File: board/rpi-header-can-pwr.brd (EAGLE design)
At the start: 65 x 56.5 mm, 31 parts, among them U1 MCP2515, X1 RJ45-8L21-S, X2 RJ45-8L21-S

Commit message: board - minor adjustments
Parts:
- removed JP3: (no value), pinhead:1X02
- added J1: (no value), SparkFun-Connectors:SCREWTERMINAL-3.5MM-2
- moved C4 2.83 mm to (55.8, 17.3), turned to 270 degrees
- moved C3 0.76 mm to (54.0, 17.4), turned to 270 degrees
- moved F3 0.50 mm to (53.5, 13.5), turned to 180 degrees
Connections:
- net GND: now also J1.1; no longer JP3.1
- net N$5: now also J1.2; no longer JP3.2
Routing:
- net N$5: track 5.37 -> 8.85 mm
- net +3V3: track 71.0 -> 67.8 mm
- net +12V: track 81.3 -> 84.0 mm
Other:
- board text added: "12V"
- board text added: "2020.05.08 v1.2"
- board text added: "FUSE 1.35A"
- board text added: "FUSE 2.5A"
- board text added: "GND"
- board text removed: "2020.05.03 v1.2"
- board text removed: "5V"
- board text removed: "5V enable"
- board text removed: "FUSE"
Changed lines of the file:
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@@
 <text x="33.1" y="44.5" size="0.8128" layer="121">C1</text>
 <text x="35.5" y="44.5" size="0.8128" layer="121">C2</text>
-<text x="56.7" y="16.2" size="0.8128" layer="121">C1</text>
-<text x="56.7" y="14.3" size="0.8128" layer="121">C2</text>
+<text x="53.5" y="14.5" size="0.8128" layer="121">C1</text>
+<text x="55.3" y="14.5" size="0.8128" layer="121">C2</text>
 <text x="5.3" y="12.2" size="0.8128" layer="121">shield</text>
 <text x="46.2" y="27.4" size="0.8128" layer="121">slope</text>
@@
 <circle x="36.8" y="34.2" radius="0.412309375" width="0.3048" layer="121"/>
 <text x="40.9" y="21.9" size="0.8128" layer="121">D2</text>
-<text x="11.6866" y="27.915" size="1.524" layer="200" font="vector" rot="R90">2020.05.03
+<text x="11.6866" y="27.915" size="1.524" layer="200" font="vector" rot="R90">2020.05.08
 v1.2</text>
 <rectangle x1="30.0314" y1="40.9822" x2="30.387" y2="41.033" layer="200" rot="R90"/>
@@
 <rectangle x1="12.3784" y1="44.0556" x2="12.5816" y2="44.1064" layer="200" rot="R90"/>
 <rectangle x1="12.4038" y1="45.5034" x2="12.5562" y2="45.5542" layer="200" rot="R90"/>
-<text x="4.5" y="41" size="1.016" layer="121" rot="R90">5V enable</text>
 <text x="16" y="46.5" size="1.016" layer="122" rot="MR180">C5</text>
 <text x="18.5" y="46.6" size="1.016" layer="122" rot="MR180">C5</text>
@@
 <wire x1="44" y1="4" x2="46" y2="4" width="0.4064" layer="121" curve="180"/>
 <wire x1="44" y1="19" x2="46" y2="19" width="0.4064" layer="121" curve="-180"/>
-<text x="3" y="44" size="1.016" layer="121">5V</text>
 <text x="9.2" y="32.3" size="0.8128" layer="121">R1</text>
-<text x="50.5" y="15" size="1.016" layer="121">FUSE</text>
+<text x="51.9" y="12.7" size="1.016" layer="121">FUSE
+1.35A</text>
 <polygon width="0.254" layer="29">
 <vertex x="16.5" y="38.5"/>
@@
 <wire x1="11.5" y1="37" x2="12" y2="36" width="0.254" layer="121"/>
 <wire x1="12" y1="36" x2="11" y2="36" width="0.254" layer="121"/>
+<text x="5" y="40.5" size="1.016" layer="121">FUSE
+2.5A</text>
+<text x="54" y="2" size="1.016" layer="121">12V</text>
+<text x="49.5" y="2" size="1.016" layer="121">GND</text>
 </plain>
 <attributes>
@@
 <attribute name="PROD_ID" value="CAP-07876" x="51.36" y="54.72" size="1.778" layer="27" rot="R270" display="off"/>
 </element>
-<element name="C3" library="rcl" package="C0603" value="100n" x="54.63" y="16.98"/>
-<element name="C4" library="rcl" package="C0603" value="1u" x="54.68" y="14.73"/>
+<element name="C3" library="rcl" package="C0603" value="100n" x="53.98" y="17.37" rot="R270"/>
+<element name="C4" library="rcl" package="C0603" value="1u" x="55.83" y="17.32" rot="R270"/>
 <element name="C6" library="rcl" package="C0603" value="1u" x="33.63" y="42.51" rot="R270"/>
 <element name="C8" library="rcl" package="C0603" value="100n" x="35.98" y="42.52" rot="R270"/>
@@
 <element name="D3" library="transistor" package="SOT23" value="BC846" x="8" y="38" rot="MR0"/>
 <element name="R4" library="rcl" package="R0603" value="1k" x="8" y="33" rot="MR270"/>
-<element name="JP3" library="pinhead" package="1X02" value="" x="53.5" y="5"/>
-<element name="F3" library="fuse" package="LITTLEFUSE" value="" x="53.5" y="13" rot="R135">
-<attribute name="OC_FARNELL" value="unknown" x="53.5" y="13" size="1.778" layer="27" rot="R135" display="off"/>
-<attribute name="MPN" value="" x="53.5" y="13" size="1.778" layer="27" rot="R135" display="off"/>
-<attribute name="OC_NEWARK" value="unknown" x="53.5" y="13" size="1.778" layer="27" rot="R135" display="off"/>
-<attribute name="MF" value="" x="53.5" y="13" size="1.778" layer="27" rot="R135" display="off"/>
+<element name="F3" library="fuse" package="LITTLEFUSE" value="" x="53.5" y="13.5" rot="R180">
+<attribute name="OC_FARNELL" value="unknown" x="53.5" y="13.5" size="1.778" layer="27" rot="R180" display="off"/>
+<attribute name="MPN" value="" x="53.5" y="13.5" size="1.778" layer="27" rot="R180" display="off"/>
+<attribute name="OC_NEWARK" value="unknown" x="53.5" y="13.5" size="1.778" layer="27" rot="R180" display="off"/>
+<attribute name="MF" value="" x="53.5" y="13.5" size="1.778" layer="27" rot="R180" display="off"/>
 </element>
 <element name="F5" library="fuse" package="TE5" value="FUSETE5" x="10" y="44" rot="R135">
@@
 <attribute name="OC_NEWARK" value="unknown" x="10" y="44" size="1.778" layer="27" rot="R135" display="off"/>
 <attribute name="MF" value="" x="10" y="44" size="1.778" layer="27" rot="R135" display="off"/>
+</element>
+<element name="J1" library="SparkFun-Connectors" package="SCREWTERMINAL-3.5MM-2" value="" x="51.2" y="7.1">
+<attribute name="PROD_ID" value="CONN-08399" x="51.2" y="7.1" size="1.778" layer="27" display="off"/>
 </element>
 </elements>
@@
 <wire x1="35.98" y1="43.37" x2="38.1079" y2="43.37" width="0.4064" layer="1"/>
 <wire x1="38.1079" y1="43.37" x2="38.32" y2="43.1579" width="0.4064" layer="1"/>
-<wire x1="53.83" y1="14.73" x2="53.83" y2="15.43" width="0.4064" layer="1"/>
-<wire x1="53.83" y1="15.43" x2="53.78" y2="16.98" width="0.4064" layer="1"/>
 <wire x1="33.63" y1="43.36" x2="35.97" y2="43.36" width="0.4064" layer="1"/>
 <wire x1="35.97" y1="43.36" x2="35.98" y2="43.37" width="0.4064" layer="1"/>
@@
 <wire x1="28.7" y1="51.22" x2="28.7" y2="43.36" width="0.4064" layer="1"/>
 <wire x1="28.7" y1="43.36" x2="33.63" y2="43.36" width="0.4064" layer="1"/>
-<wire x1="53.145" y1="20.6425" x2="53.145" y2="18.5" width="0.4064" layer="1"/>
-<wire x1="53.145" y1="18.5" x2="53.145" y2="18.115" width="0.4064" layer="1"/>
-<wire x1="53.145" y1="18.115" x2="53.78" y2="16.98" width="0.4064" layer="1"/>
 <wire x1="38.32" y1="43.1579" x2="38.32" y2="39.5" width="0.6096" layer="1"/>
 <wire x1="38.32" y1="39.5" x2="43" y2="39.5" width="0.6096" layer="1"/>
@@
 <via x="58.5" y="26.5" extent="1-16" drill="0.8" diameter="1.6764"/>
 <wire x1="58.5" y1="26.5" x2="58.5" y2="18.5" width="0.6096" layer="1"/>
-<wire x1="58.5" y1="18.5" x2="53.145" y2="18.5" width="0.6096" layer="1"/>
+<wire x1="53.145" y1="20.6425" x2="53.145" y2="18.22" width="0.4064" layer="1"/>
+<wire x1="53.145" y1="18.22" x2="53.98" y2="18.22" width="0.4064" layer="1"/>
+<wire x1="53.98" y1="18.22" x2="53.98" y2="18.17" width="0.4064" layer="1"/>
+<wire x1="53.98" y1="18.17" x2="55.83" y2="18.17" width="0.4064" layer="1"/>
+<wire x1="55.83" y1="18.17" x2="58.5" y2="18.17" width="0.4064" layer="1"/>
+<wire x1="58.5" y1="18.17" x2="58.5" y2="18.5" width="0.4064" layer="1"/>
 </signal>
 <signal name="GND">
@@
 <via x="19.6" y="36.3" extent="1-16" drill="0.6"/>
 <via x="17" y="36.3" extent="1-16" drill="0.6"/>
-<via x="59.3" y="13.5" extent="1-16" drill="0.6"/>
+<via x="62.3" y="8" extent="1-16" drill="0.6"/>
 <via x="47.7" y="4" extent="1-16" drill="0.6"/>
 <via x="37.3" y="18.5" extent="1-16" drill="0.6"/>
@@
 <contactref element="R4" pad="2"/>
 <contactref element="D3" pad="2"/>
-<contactref element="JP3" pad="1"/>
 <via x="40.8" y="28.7" extent="1-16" drill="0.6"/>
 <via x="38.3" y="28.7" extent="1-16" drill="0.6"/>
@@
 <via x="61.3" y="27.5" extent="1-16" drill="0.6"/>
 <via x="48.3" y="7" extent="1-16" drill="0.6"/>
-<via x="48.3" y="13.5" extent="1-16" drill="0.6"/>
+<via x="47.8" y="10" extent="1-16" drill="0.6"/>
 <via x="40.3" y="37" extent="1-16" drill="0.6"/>
 <via x="44.3" y="37" extent="1-16" drill="0.6"/>
@@
 <via x="51.3" y="45" extent="1-16" drill="0.6"/>
 <via x="26.8" y="42.5" extent="1-16" drill="0.6"/>
+<contactref element="J1" pad="1"/>
 </signal>
 <signal name="CAN_TX">
@@
 <wire x1="33" y1="25.778828125" x2="38.5" y2="23" width="1.4224" layer="16"/>
 <wire x1="38.5" y1="23" x2="39.5" y2="22" width="1.4224" layer="16"/>
-<wire x1="39.5" y1="22" x2="48" y2="22" width="1.4224" layer="16"/>
-<wire x1="48" y1="22" x2="48.25" y2="21.75" width="1.4224" layer="16"/>
 <contactref element="F3" pad="2"/>
-<wire x1="49.907896875" y1="16.5921" x2="48.25" y2="18.249996875" width="1.4224" layer="16"/>
-<wire x1="48.25" y1="18.249996875" x2="48.25" y2="21.75" width="1.4224" layer="16"/>
+<wire x1="48.42" y1="13.5" x2="48.42" y2="22" width="1.4224" layer="16"/>
+<wire x1="48.42" y1="22" x2="39.5" y2="22" width="1.4224" layer="16"/>
 </signal>
 <signal name="N$1">
@@
 </signal>
 <signal name="N$5">
-<contactref element="JP3" pad="2"/>
 <contactref element="F3" pad="1"/>
-<wire x1="54.77" y1="5" x2="54.77" y2="7.085796875" width="1.4224" layer="16"/>
-<wire x1="54.77" y1="7.085796875" x2="57.0921" y2="9.407896875" width="1.4224" layer="16"/>
+<contactref element="J1" pad="2"/>
+<wire x1="56.085796875" y1="7.085796875" x2="58.5" y2="9.5" width="1.4224" layer="16"/>
+<wire x1="58.5" y1="9.5" x2="58.5" y2="13.42" width="1.4224" layer="16"/>
+<wire x1="58.5" y1="13.42" x2="58.58" y2="13.5" width="1.4224" layer="16"/>
+<wire x1="54.7" y1="7.1" x2="54.7" y2="7.085796875" width="1.4224" layer="16"/>
+<wire x1="54.7" y1="7.085796875" x2="56.085796875" y2="7.085796875" width="1.4224" layer="16"/>
 </signal>
 <signal name="N$8">

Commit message: add tamper
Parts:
- added C12: 10nF, eagle-ltspice:C0402
- added D18: BAS70-04, diode:SOT23
- added GND84: (no value), SparkFun-Connectors:SCREWTERMINAL-3.5MM-2
- added R59: 10k, rcl:R0402
- added R60, R61: 100, rcl:R0402
- added R62: 1k, rcl:R0402
- moved R25 2.27 mm to (6.76, 7.99), turned to 180 degrees
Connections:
- removed net GPIO17: RPI1.11
- removed net GPIO5: RPI1.29
- new net ASDASD: D18.3, R61.1, R62.2
- new net N$10: GND84.2, R60.1
- new net N$11: C12.2, GND84.1, R59.1, R62.1
- new net TAMPER: R61.2, RPI1.11
- net +3V3: now also D18.2, R60.2
- net GND: now also C12.1, D18.1, R59.2
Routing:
- net +3V3: track 67.8 -> 123.6 mm, vias 2 -> 3
- net TAMPER: track 0.00 -> 34.1 mm
- net N$11: track 0.00 -> 12.9 mm
- net ASDASD: track 0.00 -> 4.52 mm
- net N$10: track 0.00 -> 3.85 mm
- net N$20: track 41.0 -> 39.1 mm
- net GND: vias 133 -> 132
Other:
- board text added: "C9"
- board text added: "D4"
- board text added: "R15"
- board text added: "R16"
- board text added: "R17"

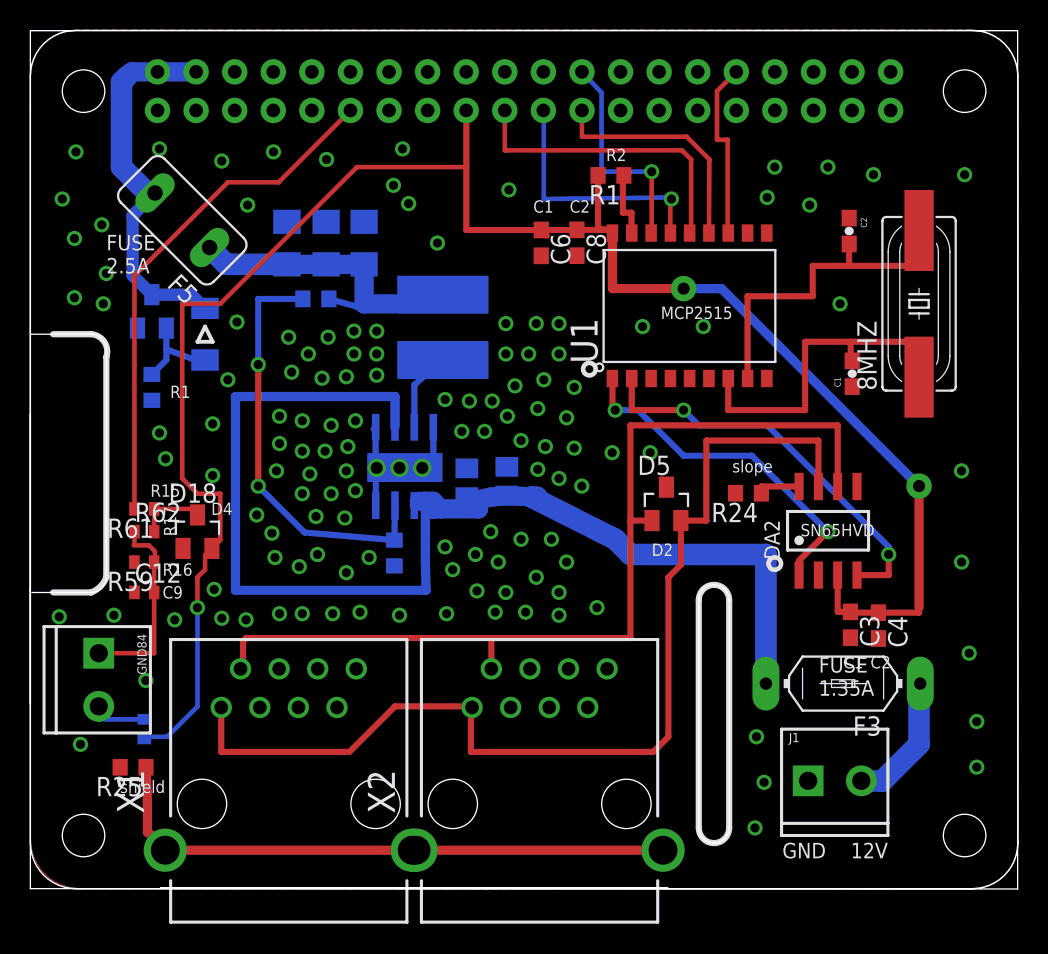
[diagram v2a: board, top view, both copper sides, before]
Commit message: power over can
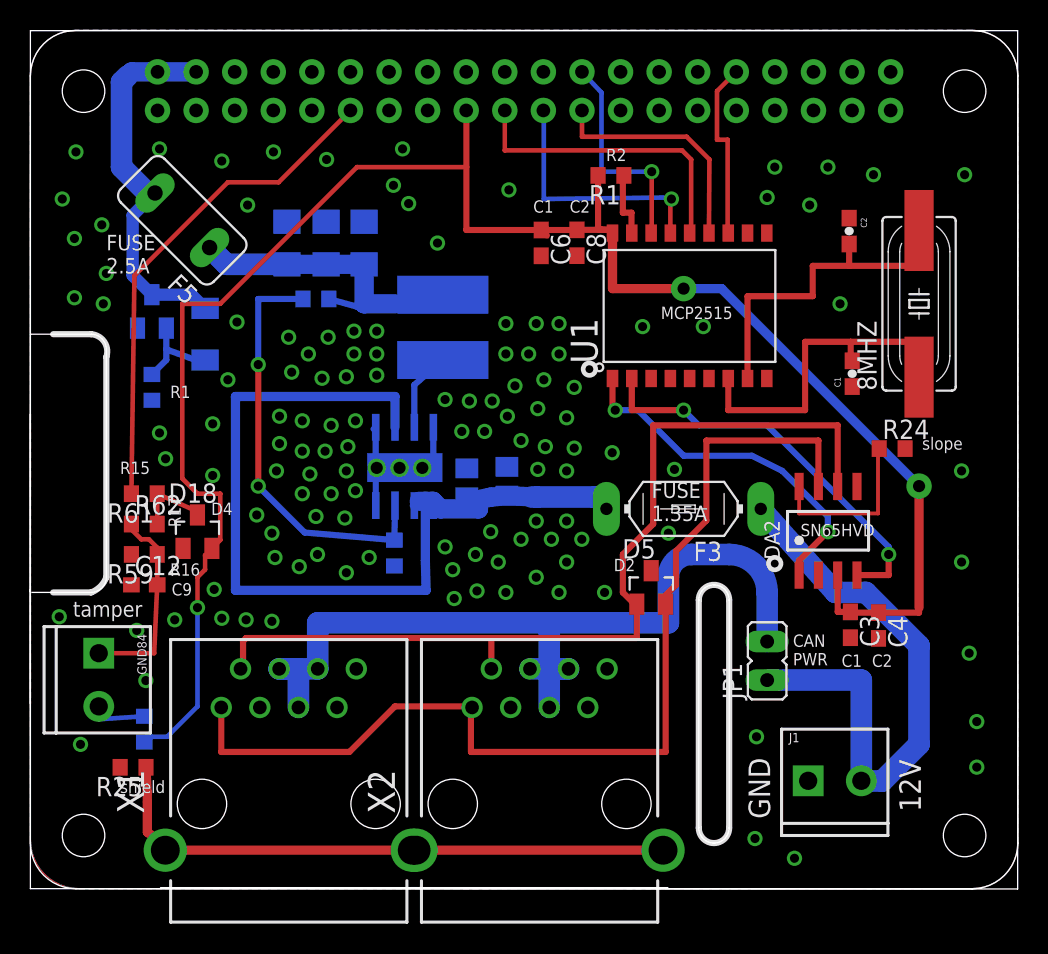
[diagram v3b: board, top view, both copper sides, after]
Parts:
- added JP1: (no value), jumper:JP1
- C12: device eagle-ltspice:C0402 -> eagle-ltspice:C0603
- R59, R60, R61, R62: device rcl:R0402 -> rcl:R0603
- moved F3 15.6 mm to (43.0, 25.0)
- moved R24 9.91 mm to (56.7, 29.0), turned to 0 degrees
- moved D5 5.59 mm to (40.9, 19.8)
- moved R61 1.00 mm to (7.50, 26.0)
- moved C12 0.50 mm to (7.50, 20.0)
- moved R59 0.50 mm to (7.50, 22.0)
- moved R62 0.50 mm to (7.50, 24.0)
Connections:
- removed net N$5: F3.1, J1.2
- new net PRE_FUSE_12V: F3.1, J1.2, JP1.1
- new net RJ45_12V: JP1.2, X1.4, X1.5, X1.6, X2.4, X2.5, X2.6
- net GND: now also X1.8, X2.8
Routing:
- net RJ45_12V: track 0.00 -> 56.2 mm
- net PRE_FUSE_12V: track 0.00 -> 38.5 mm
- net +12V: track 84.0 -> 63.9 mm
- net N$5: track 8.85 -> 0.00 mm
- net N$17: track 2.93 -> 11.3 mm
- net CAN_L: track 62.6 -> 61.4 mm
- net TAMPER: track 34.1 -> 33.1 mm
- net ASDASD: track 4.52 -> 5.03 mm
- net CAN_H: track 69.0 -> 68.5 mm
- net GND: vias 132 -> 128
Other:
- board text added: "CAN PWR"
- board text added: "D6"
- board text added: "R5"
- board text added: "T3"
- board text added: "can rpi header 2020.06.12 v1.3"
- board text added: "tamper"
- board text removed: "2020.05.08 v1.2"

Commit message: extra fuse for power over can
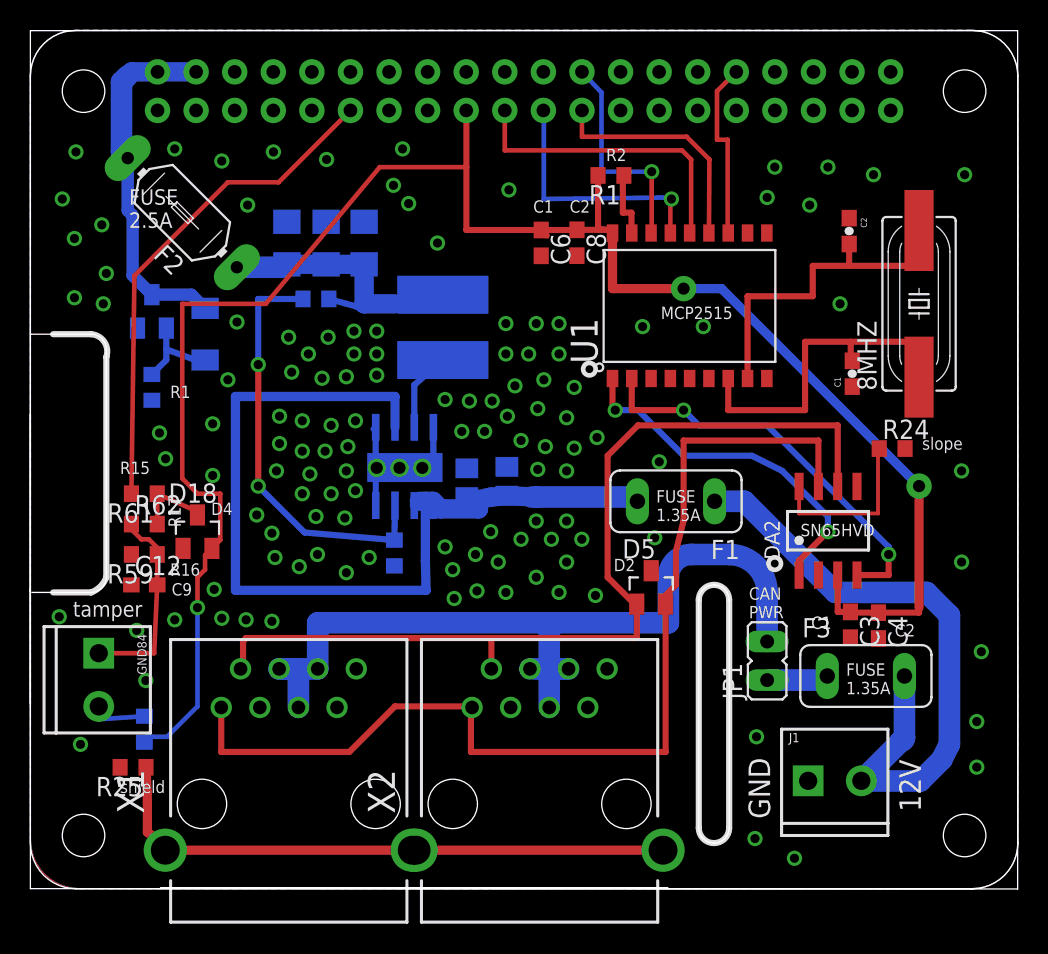
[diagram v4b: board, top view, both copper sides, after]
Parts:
- removed F5: FUSETE5, fuse:TE5
- added F1: FUSETE5, fuse:TE5
- added F2: FUSELITTLEFUSE, fuse:LITTLEFUSE
- F3: value (none) -> FUSETE5; device fuse:LITTLEFUSE -> fuse:TE5
- moved F3 16.3 mm to (55.0, 14.0), turned to 0 degrees
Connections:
- new net N$5: F3.1, JP1.1
- net +12V: now also F1.2; no longer F3.2
- net 5V: now also F2.2; no longer F5.2
- net N$8: now also F2.1; no longer F5.1
- net PRE_FUSE_12V: now also F1.1, F3.2; no longer F3.1, JP1.1
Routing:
- net N$5: track 0.00 -> 4.07 mm
- net PRE_FUSE_12V: track 38.5 -> 42.5 mm
- net N$8: track 21.3 -> 19.1 mm
- net +12V: track 63.9 -> 65.8 mm
- net 5V: track 25.4 -> 23.9 mm
- net CAN_L: track 61.4 -> 62.8 mm
- net CAN_H: track 68.5 -> 69.3 mm
